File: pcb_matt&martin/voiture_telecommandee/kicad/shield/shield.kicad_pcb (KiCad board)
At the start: 2 copper layers, 100 x 100 mm, 13 parts, among them J2 Bluetooth, U1 COM-09032

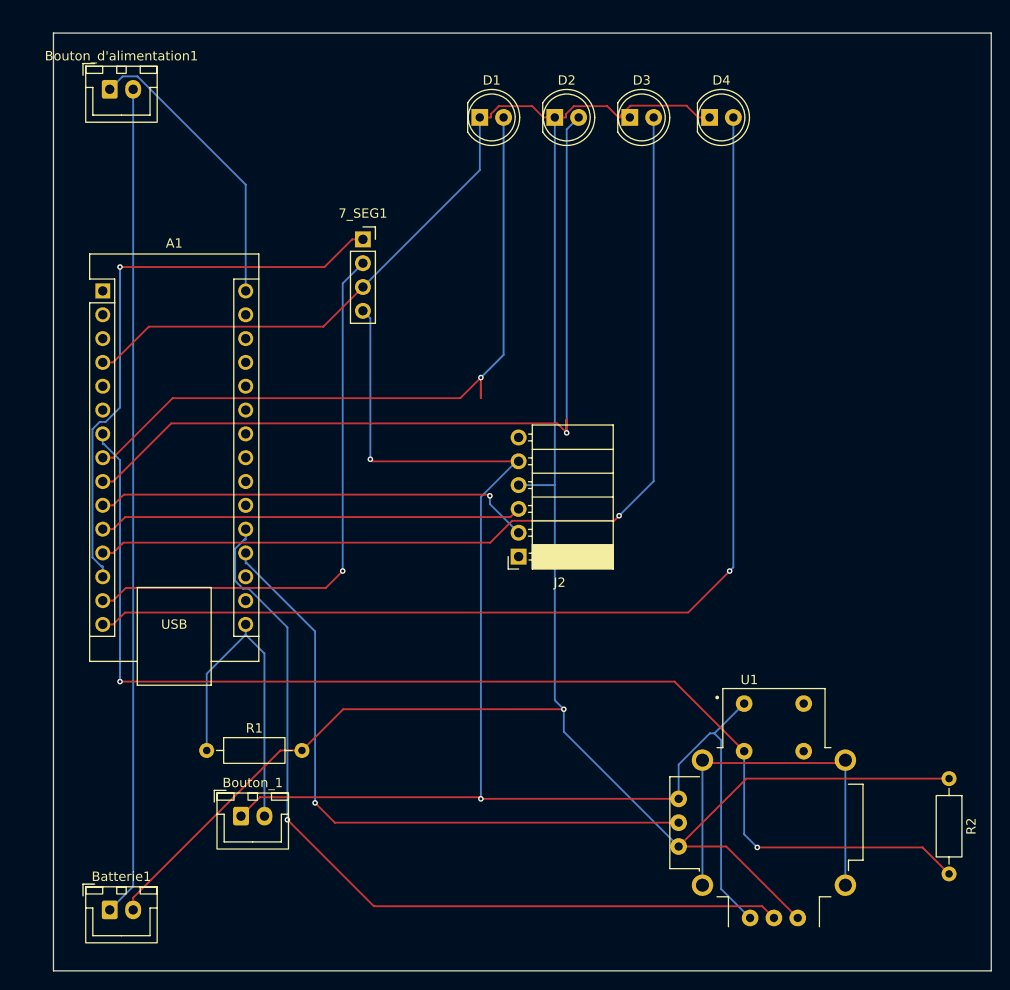
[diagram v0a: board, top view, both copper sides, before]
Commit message: Résolu Issue #12
J'ai tout simplement mis le symbole sur l'Arduino et rerouté et tout le tralala
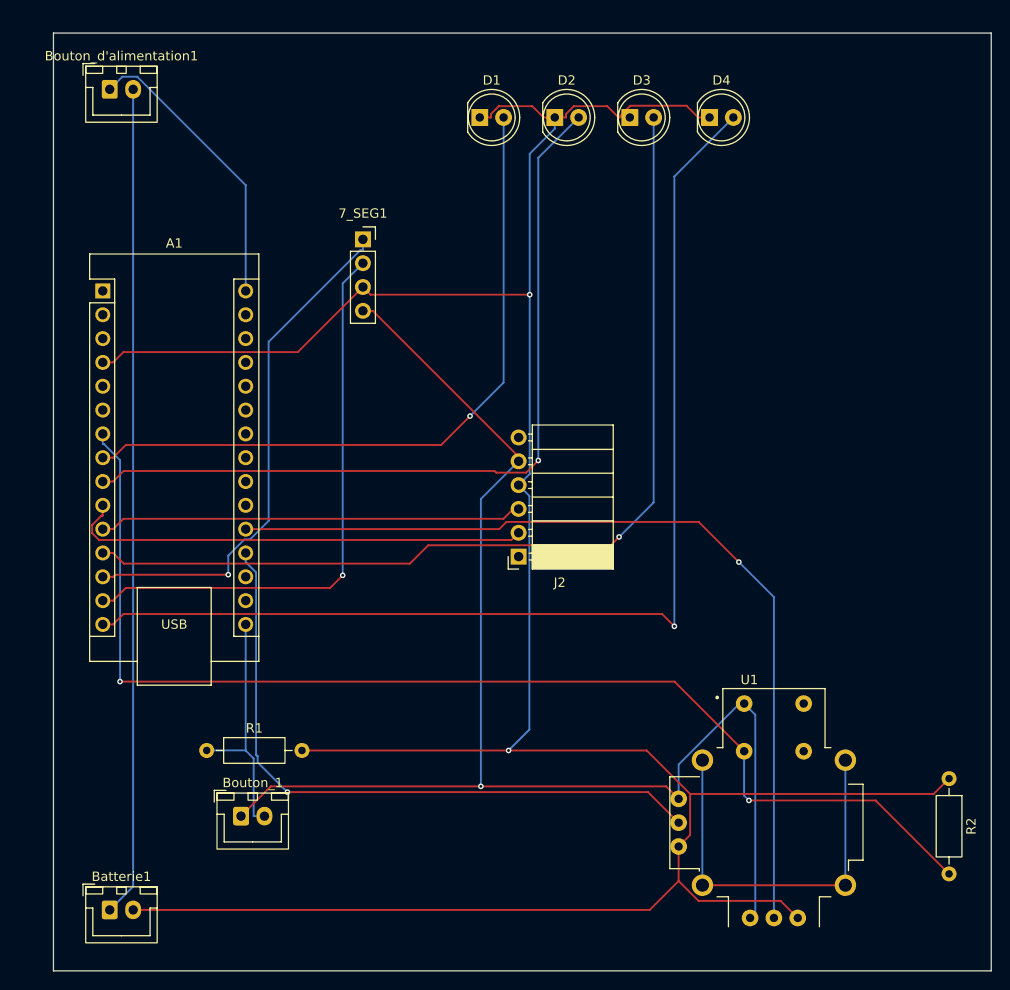
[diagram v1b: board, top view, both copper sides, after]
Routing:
- net GND: track 273.8 -> 304.0 mm, vias 1 -> 2
- net /BTN_1: track 35.3 -> 26.1 mm
- net /LED_1: track 81.4 -> 74.3 mm
- net +5V: track 152.0 -> 145.3 mm, vias 2 -> 1
- net /7_SEG_CLK: track 62.3 -> 55.7 mm
- net /LED_2: track 92.3 -> 85.9 mm
- net /H2: track 90.4 -> 94.2 mm
- net /BTH_RX: track 47.0 -> 49.6 mm, vias 1 -> 0
- net /<NO NET>: track 129.3 -> 126.9 mm
- net /LED_3: track 100.7 -> 103.0 mm
- net /V2: track 69.4 -> 70.7 mm
- net /LED_4: track 117.7 -> 118.8 mm

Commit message: Résolution de l'issue #11
Pas sûr-sûr que fallait faire comme ça mais bon (https://github.com/Y159753/v-rification_pcb_manette_les_experts/issues/11#issuecomment-3921551236) Donc du coup j'ai mis le signe gnd sur la 2eme broche gnd de l'Arduino.
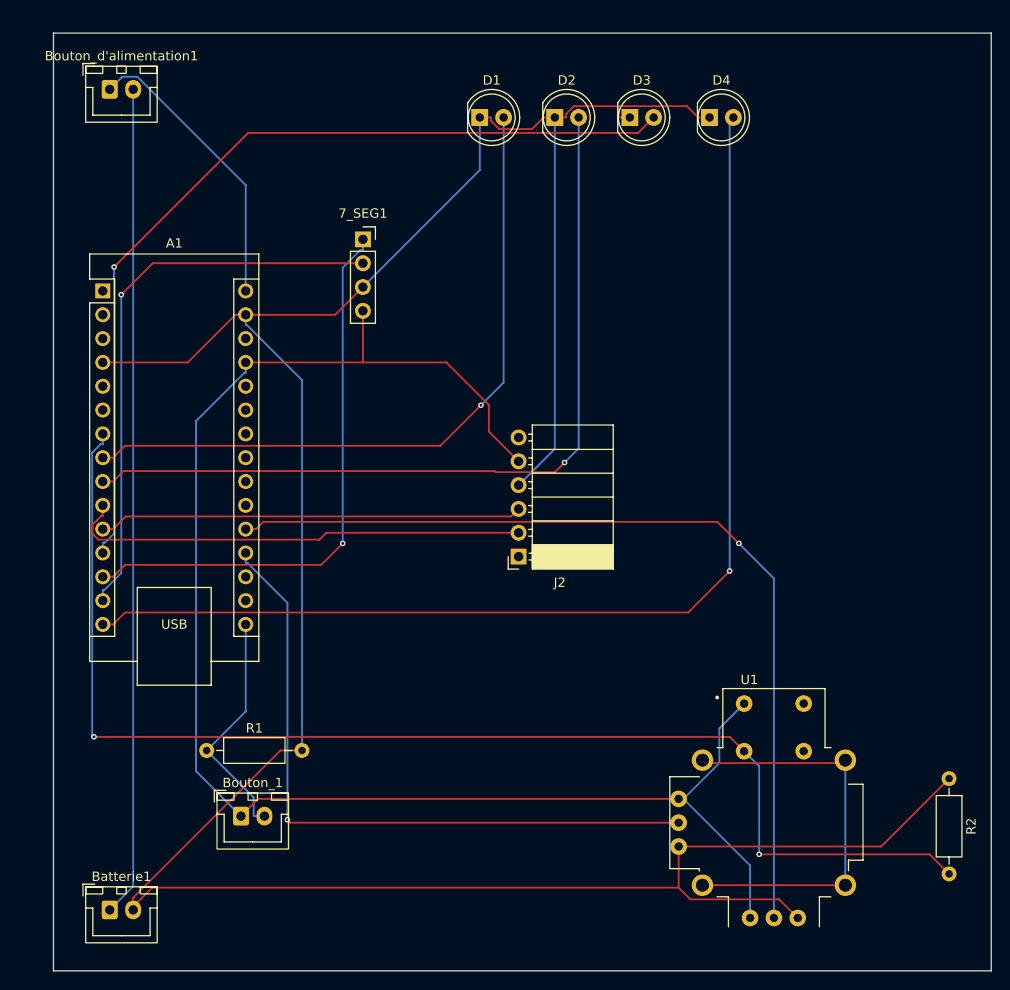
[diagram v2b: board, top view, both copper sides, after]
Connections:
- A1 pad 27: unconnected-(A1-+5V-Pad27) -> +5V
- A1 pad 29: unconnected-(A1-GND-Pad29) -> GND
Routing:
- net +5V: track 145.3 -> 169.7 mm, vias 1 -> 0
- net /<NO NET>: track 126.9 -> 136.5 mm
- net /LED_3: track 103.0 -> 95.3 mm
- net /7_SEG_CLK: track 55.7 -> 60.5 mm
- net GND: track 304.0 -> 308.6 mm, vias 2 -> 0
- net Earth: track 41.9 -> 44.1 mm
- net /LED_2: track 85.9 -> 87.9 mm
- net /V2: track 70.7 -> 72.3 mm
- net /H2: track 94.2 -> 95.3 mm
- net /LED_4: track 118.8 -> 117.7 mm
- net /BTN_1: track 26.1 -> 25.4 mm

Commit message: bon euuuuu y'a bcp de changements
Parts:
- ARDUINO1: renamed from A1; moved to B.Cu
- Batterie1, R1, R2: moved to B.Cu
- Bouton1: renamed from Bouton_1; moved to B.Cu
- Btn_alim1: renamed from Bouton_d'alimentation1; moved to B.Cu
- moved R2 71.9 mm to (116.4, 104.0), turned to 0 degrees
- moved Btn_alim1 67.2 mm to (128.0, 114.5), turned to 180 degrees
- moved Bluetooth1 39.0 mm to (100.0, 116.6)
- moved Batterie1 38.0 mm to (118.0, 114.5), turned to 180 degrees
- moved Bouton1 36.0 mm to (138.2, 114.5), turned to 180 degrees
- moved Joystick1 28.9 mm to (164.0, 105.8)
- moved R1 22.1 mm to (116.4, 108.5)
- moved ARDUINO1 19.7 mm to (99.5, 96.7)
- moved LED1 3.00 mm to (130.5, 60.0)
- moved LED2 3.00 mm to (138.5, 60.0)
- moved LED3 3.00 mm to (146.5, 60.0)
- moved LED4 3.00 mm to (155.0, 60.0)
- renumbered J2 to Bluetooth1, U1 to Joystick1, D1 to LED1, D2 to LED2, D3 to LED3, D4 to LED4
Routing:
- net GND: track 308.6 -> 188.8 mm
- net /BTN_BATT_IN: track 88.5 -> 7.50 mm
- net /<NO NET>: track 136.5 -> 76.4 mm, vias 2 -> 0
- net /LED_4: track 117.7 -> 60.4 mm, vias 1 -> 0
- net /BTN_1: track 25.4 -> 72.8 mm
- net /LED_3: track 95.3 -> 56.6 mm, vias 1 -> 0
- net +5V: track 169.7 -> 132.8 mm, vias 0 -> 1
- net /7_SEG_CLK: track 60.5 -> 24.1 mm, vias 1 -> 0
- net /LED_2: track 87.9 -> 57.4 mm
- net /7_SEG_DIO: track 60.7 -> 31.4 mm, vias 1 -> 0
- net /LED_1: track 74.3 -> 51.4 mm
- net /BTN_BATT_OUT: track 31.1 -> 23.3 mm
- net /BTH_RX: track 49.6 -> 41.9 mm
- net /BTH_TX: track 45.2 -> 41.6 mm
- net /H2: track 95.3 -> 91.9 mm
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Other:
- board size 100 x 100 mm -> 88 x 77.5 mm
- board text added: "5V"
- board text added: "<->"
- board text added: "A0"
- board text added: "A1"
- board text added: "D10"
- board text added: "D11"
- board text added: "D12"
- board text added: "D13"
- board text added: "D4"
- board text added: "D5"
- board text added: "D6"
- board text added: "D7"
- board text added: "D8"
- board text added: "D9"
- board text added: "GND"
- board text added: "V.IN"
